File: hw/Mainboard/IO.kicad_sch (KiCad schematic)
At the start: 6 parts, among them U11 W65C21N, U12 W65C22N, U13 W65C21N

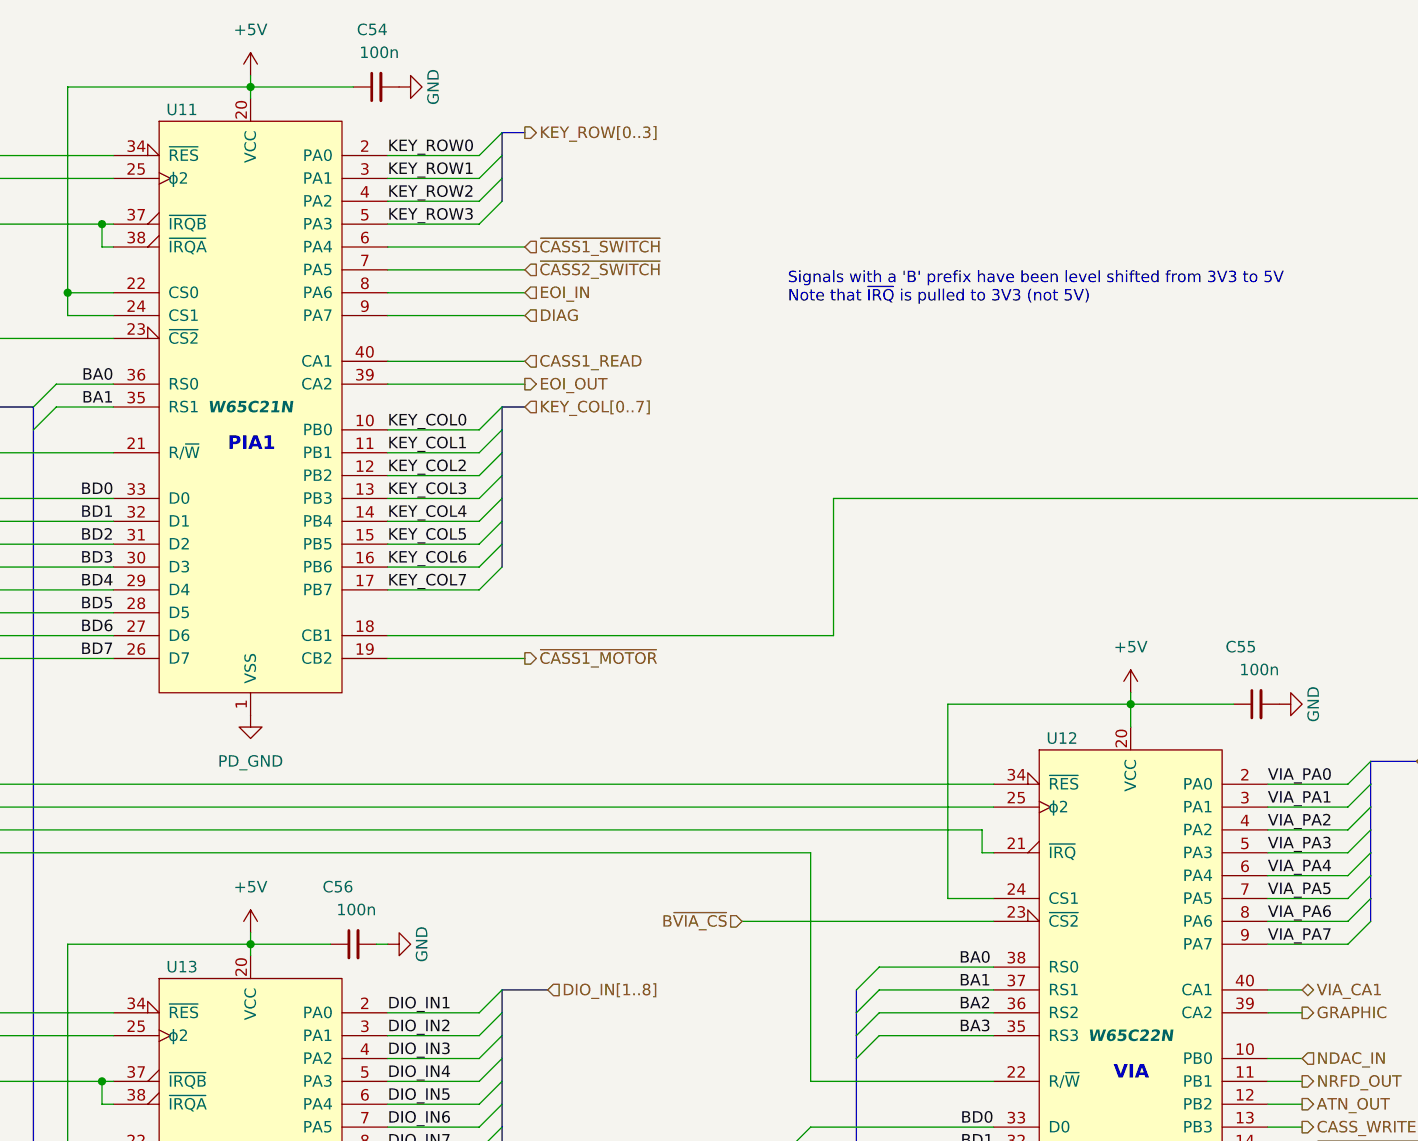
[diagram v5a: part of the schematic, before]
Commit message: hw: renumber J* refs to match PET connectors
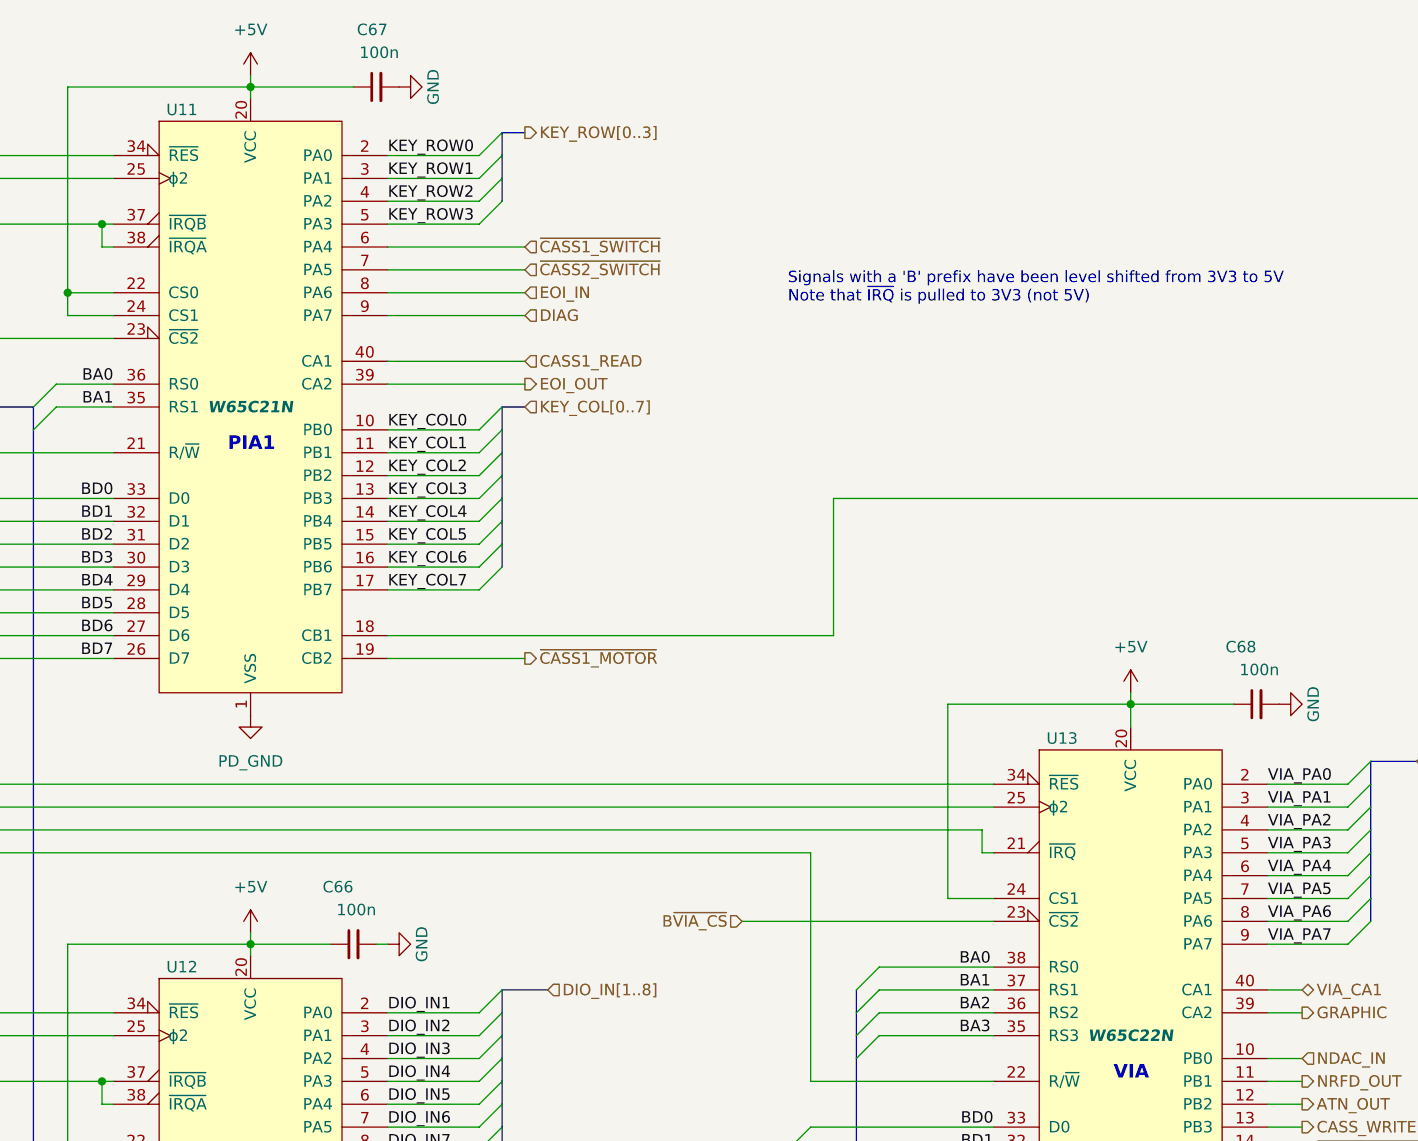
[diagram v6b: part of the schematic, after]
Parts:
- renumbered C56 to C66, C54 to C67, C55 to C68, U13 to U12, U12 to U13
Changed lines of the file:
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@@
   (symbol (lib_id "Mainboard-rescue:W65C21NxP-PET") (at 86.36 153.67 0) (unit 1)
     (in_bom yes) (on_board yes)
-    (property "Reference" "U13" (id 0) (at 78.74 120.65 0))
+    (property "Reference" "U12" (id 0) (at 78.74 120.65 0))
     (property "Value" "W65C21N" (id 1) (at 86.36 153.67 0)
       (effects (font (size 1.27 1.27) bold italic))
@@
   (symbol (lib_id "Mainboard-rescue:W65C22NxP-PET") (at 184.15 128.27 0) (unit 1)
     (in_bom yes) (on_board yes)
-    (property "Reference" "U12" (id 0) (at 176.53 95.25 0))
+    (property "Reference" "U13" (id 0) (at 176.53 95.25 0))
     (property "Value" "W65C22N" (id 1) (at 184.15 128.27 0)
       (effects (font (size 1.27 1.27) bold italic))
@@
   (symbol (lib_id "Device:C_Small") (at 97.79 118.11 90) (unit 1)
     (in_bom yes) (on_board yes)
-    (property "Reference" "C56" (id 0) (at 97.79 111.76 90)
+    (property "Reference" "C66" (id 0) (at 97.79 111.76 90)
       (effects (font (size 1.27 1.27)) (justify left))
     )
@@
   (symbol (lib_id "Device:C_Small") (at 100.33 22.86 90) (unit 1)
     (in_bom yes) (on_board yes)
-    (property "Reference" "C54" (id 0) (at 101.6 16.51 90)
+    (property "Reference" "C67" (id 0) (at 101.6 16.51 90)
       (effects (font (size 1.27 1.27)) (justify left))
     )
@@
   (symbol (lib_id "Device:C_Small") (at 198.12 91.44 90) (unit 1)
     (in_bom yes) (on_board yes)
-    (property "Reference" "C55" (id 0) (at 198.12 85.09 90)
+    (property "Reference" "C68" (id 0) (at 198.12 85.09 90)
       (effects (font (size 1.27 1.27)) (justify left))
     )
@@
   (symbol (lib_id "PET:PD_GND") (at 86.36 187.96 0) (unit 1)
     (in_bom yes) (on_board yes) (fields_autoplaced)
-    (property "Reference" "#PWR097" (id 0) (at 86.36 194.31 0)
+    (property "Reference" "#PWR091" (id 0) (at 86.36 194.31 0)
       (effects (font (size 1.27 1.27)) hide)
     )
@@
   (symbol (lib_id "power:+5V") (at 86.36 21.59 0) (unit 1)
     (in_bom yes) (on_board yes)
-    (property "Reference" "#PWR089" (id 0) (at 86.36 25.4 0)
+    (property "Reference" "#PWR088" (id 0) (at 86.36 25.4 0)
       (effects (font (size 1.27 1.27)) hide)
     )
@@
   (symbol (lib_id "power:GND") (at 101.6 118.11 90) (unit 1)
     (in_bom yes) (on_board yes)
-    (property "Reference" "#PWR095" (id 0) (at 107.95 118.11 0)
+    (property "Reference" "#PWR092" (id 0) (at 107.95 118.11 0)
       (effects (font (size 1.27 1.27)) hide)
     )
@@
   (symbol (lib_id "power:GND") (at 102.87 22.86 90) (unit 1)
     (in_bom yes) (on_board yes)
-    (property "Reference" "#PWR090" (id 0) (at 109.22 22.86 0)
+    (property "Reference" "#PWR093" (id 0) (at 109.22 22.86 0)
       (effects (font (size 1.27 1.27)) hide)
     )
@@
   (symbol (lib_id "PET:PD_GND") (at 184.15 162.56 0) (unit 1)
     (in_bom yes) (on_board yes) (fields_autoplaced)
-    (property "Reference" "#PWR096" (id 0) (at 184.15 168.91 0)
+    (property "Reference" "#PWR095" (id 0) (at 184.15 168.91 0)
       (effects (font (size 1.27 1.27)) hide)
     )
@@
   (symbol (lib_id "PET:PD_GND") (at 86.36 92.71 0) (unit 1)
     (in_bom yes) (on_board yes) (fields_autoplaced)
-    (property "Reference" "#PWR093" (id 0) (at 86.36 99.06 0)
+    (property "Reference" "#PWR089" (id 0) (at 86.36 99.06 0)
       (effects (font (size 1.27 1.27)) hide)
     )
@@
   (symbol (lib_id "power:+5V") (at 86.36 116.84 0) (unit 1)
     (in_bom yes) (on_board yes)
-    (property "Reference" "#PWR094" (id 0) (at 86.36 120.65 0)
+    (property "Reference" "#PWR090" (id 0) (at 86.36 120.65 0)
       (effects (font (size 1.27 1.27)) hide)
     )
@@
   (symbol (lib_id "power:+5V") (at 184.15 90.17 0) (unit 1)
     (in_bom yes) (on_board yes) (fields_autoplaced)
-    (property "Reference" "#PWR091" (id 0) (at 184.15 93.98 0)
+    (property "Reference" "#PWR094" (id 0) (at 184.15 93.98 0)
       (effects (font (size 1.27 1.27)) hide)
     )
@@
   (symbol (lib_id "power:GND") (at 200.66 91.44 90) (unit 1)
     (in_bom yes) (on_board yes)
-    (property "Reference" "#PWR092" (id 0) (at 207.01 91.44 0)
-      (effects (font (size 1.27 1.27)) hide)
-    )
+    (property "Reference" "#PWR096" (id 0) (at 207.01 91.44 0)
+      (effects (font (size 1.27 1.27)) hide)
+    )

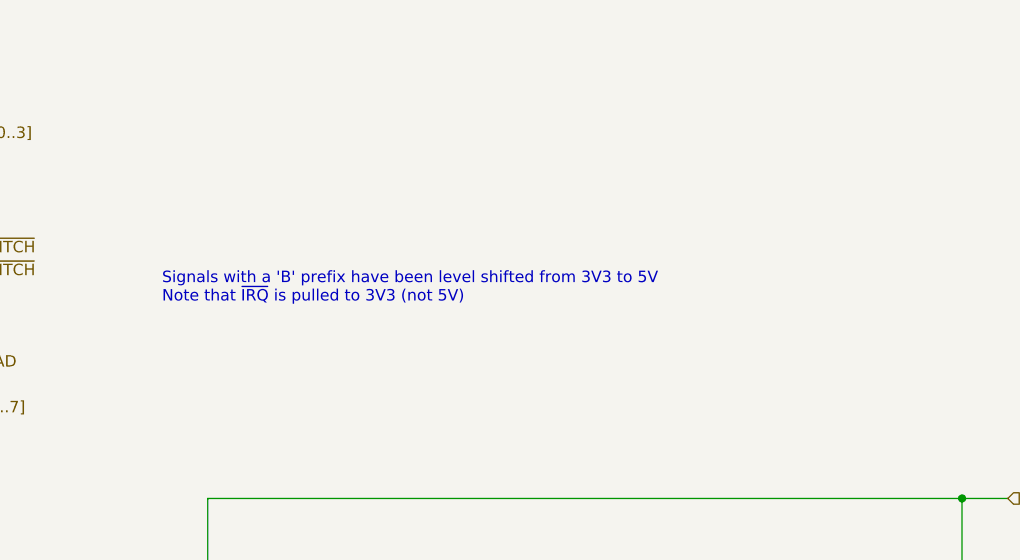
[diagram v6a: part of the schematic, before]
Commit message: hw: comments in schematics
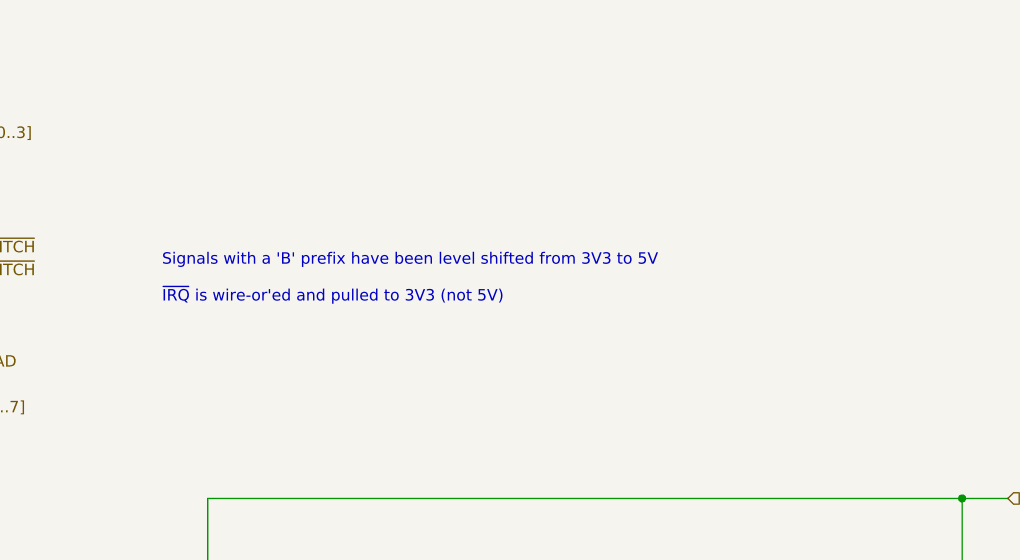
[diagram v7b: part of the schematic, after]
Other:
- note added: "Signals with a 'B' prefix have been level shifted from 3V3 to 5V ~{IRQ} is wire-or'ed and pulled to 3V3 (not 5V)"
- note removed: "Signals with a 'B' prefix have been level shifted from 3V3 to 5V Note that ~{IRQ} is pulled to 3V3 (not 5V)"
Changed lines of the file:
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@@
     (effects (font (size 1.5 1.5) (thickness 0.8) bold) (justify left bottom))
   )
-  (text "Signals with a 'B' prefix have been level shifted from 3V3 to 5V\nNote that ~{IRQ} is pulled to 3V3 (not 5V)"
+  (text "Signals with a 'B' prefix have been level shifted from 3V3 to 5V\n\n~{IRQ} is wire-or'ed and pulled to 3V3 (not 5V)"
     (at 146.05 46.99 0)
     (effects (font (size 1.27 1.27)) (justify left bottom))
